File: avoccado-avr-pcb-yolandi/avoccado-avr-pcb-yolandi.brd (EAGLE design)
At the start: 50 x 50 mm, 55 parts, among them Q1 16MHz, Q2 FET, U2 MCP73831

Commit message: wip silkscreen
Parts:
- moved TP4 1.52 mm to (15.2, 27.4)
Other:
- board text added: "AO"
- board text added: "AVOCCADO YOLANDI"
- board text added: "CK"
- board text added: "ETEMU.COM 2O15"
- board text added: "MI"
- board text added: "MO"
- board text added: "RS"
- board text added: "V1"
- board text added: "VC"
- board text added: "VIBR"
- board text removed: "3V"
- board text removed: "AVOCCADO YOLANDI V1"
- board text removed: "RST"
- board text removed: "Vcc"
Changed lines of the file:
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@@
 <layer number="19" name="Unrouted" color="6" fill="1" visible="yes" active="yes"/>
 <layer number="20" name="Dimension" color="15" fill="1" visible="yes" active="yes"/>
-<layer number="21" name="tPlace" color="16" fill="1" visible="yes" active="yes"/>
+<layer number="21" name="tPlace" color="16" fill="1" visible="no" active="yes"/>
 <layer number="22" name="bPlace" color="14" fill="1" visible="yes" active="yes"/>
 <layer number="23" name="tOrigins" color="15" fill="1" visible="yes" active="yes"/>
@@
 <layer number="27" name="tValues" color="7" fill="1" visible="no" active="yes"/>
 <layer number="28" name="bValues" color="7" fill="1" visible="no" active="yes"/>
-<layer number="29" name="tStop" color="7" fill="3" visible="yes" active="yes"/>
-<layer number="30" name="bStop" color="7" fill="6" visible="yes" active="yes"/>
+<layer number="29" name="tStop" color="7" fill="3" visible="no" active="yes"/>
+<layer number="30" name="bStop" color="7" fill="6" visible="no" active="yes"/>
 <layer number="31" name="tCream" color="7" fill="4" visible="no" active="yes"/>
 <layer number="32" name="bCream" color="7" fill="5" visible="no" active="yes"/>
@@
 <wire x1="50" y1="50" x2="0" y2="50" width="0.2032" layer="20"/>
 <text x="27.026" y="15.584" size="0.8128" layer="21" ratio="12">9</text>
-<text x="10.414" y="23.114" size="0.8128" layer="21" ratio="12">8</text>
-<text x="12.954" y="23.114" size="0.8128" layer="21" ratio="12">7</text>
-<text x="15.494" y="23.114" size="0.8128" layer="21" ratio="12">6</text>
-<text x="18.034" y="23.114" size="0.8128" layer="21" ratio="12">5</text>
 <text x="26.899" y="21.272" size="0.8128" layer="21" ratio="12">4</text>
 <text x="22.835" y="25.336" size="0.8128" layer="21" ratio="12">VIB</text>
-<text x="21.844" y="14.224" size="0.8128" layer="21" ratio="12" rot="SR90">RX</text>
-<text x="21.844" y="11.684" size="0.8128" layer="21" ratio="12" rot="SR90">TX</text>
 <text x="32.972" y="38.931" size="0.8128" layer="21" ratio="12">BAT</text>
-<text x="20.066" y="18.288" size="0.8128" layer="21" ratio="12" rot="SR0">Vcc</text>
 <text x="37.059" y="28.892" size="0.8128" layer="21" ratio="12">A3</text>
 <text x="37.059" y="26.352" size="0.8128" layer="21" ratio="12">A2</text>
@@
 <text x="37.059" y="16.192" size="0.8128" layer="21" ratio="12">12</text>
 <text x="37.059" y="13.652" size="0.8128" layer="21" ratio="12">11</text>
-<text x="21.844" y="9.652" size="0.8128" layer="21" ratio="12" rot="R90">DT</text>
 <rectangle x1="3.912" y1="0.852" x2="6.452" y2="4.408" layer="25"/>
 <rectangle x1="15.35" y1="25.998" x2="18.906" y2="28.538" layer="25"/>
@@
 <circle x="14.732" y="23.622" radius="0.2032" width="0.4064" layer="29"/>
 <circle x="17.272" y="23.622" radius="0.2032" width="0.4064" layer="29"/>
-<text x="21.844" y="7.112" size="0.8128" layer="21" ratio="12" rot="SR90">3V</text>
-<text x="6.858" y="3.556" size="0.8128" layer="21" ratio="12" rot="SR0">Vb</text>
-<text x="14.986" y="2.032" size="0.8128" layer="21" ratio="12" rot="SR0">Vin</text>
-<text x="3.302" y="3.556" size="0.8128" layer="21" ratio="12" rot="SR0">VIB</text>
-<text x="9.271" y="22.352" size="0.508" layer="21" font="vector">AVOCCADO YOLANDI V1</text>
-<text x="10.414" y="11.43" size="0.6096" layer="21" font="vector">AVOCCADO YOLANDI V1</text>
-<text x="7.112" y="13.97" size="0.6096" layer="21" ratio="10" rot="SR0" align="center-left">RST</text>
+<text x="11.6078" y="22.352" size="0.508" layer="21" font="vector">ETEMU.COM 2O15</text>
+<text x="11.684" y="11.557" size="0.6096" layer="21" font="vector" align="center-left">AVOCCADO YOLANDI</text>
+<text x="7.112" y="13.97" size="0.6096" layer="21" ratio="10" rot="SR0" align="center-left">RS</text>
+<wire x1="6.858" y1="13.97" x2="6.604" y2="13.97" width="0.127" layer="21"/>
+<wire x1="6.604" y1="13.97" x2="6.35" y2="14.224" width="0.127" layer="21"/>
+<text x="7.112" y="16.51" size="0.6096" layer="21" ratio="10" rot="SR0" align="center-left">MO</text>
+<wire x1="6.858" y1="16.51" x2="6.604" y2="16.51" width="0.127" layer="21"/>
+<wire x1="6.604" y1="16.51" x2="6.35" y2="16.764" width="0.127" layer="21"/>
+<text x="7.112" y="19.05" size="0.6096" layer="21" ratio="10" rot="SR0" align="center-left">CK</text>
+<wire x1="6.858" y1="19.05" x2="6.604" y2="19.05" width="0.127" layer="21"/>
+<wire x1="6.604" y1="19.05" x2="6.35" y2="19.304" width="0.127" layer="21"/>
+<text x="7.112" y="21.59" size="0.6096" layer="21" ratio="10" rot="SR0" align="center-left">MI</text>
+<wire x1="6.858" y1="21.59" x2="6.604" y2="21.59" width="0.127" layer="21"/>
+<wire x1="6.604" y1="21.59" x2="6.35" y2="21.844" width="0.127" layer="21"/>
+<text x="7.112" y="11.557" size="0.6096" layer="21" ratio="10" rot="SR0" align="center-left">A3</text>
+<wire x1="6.858" y1="11.43" x2="6.604" y2="11.43" width="0.127" layer="21"/>
+<wire x1="6.604" y1="11.43" x2="6.35" y2="11.684" width="0.127" layer="21"/>
+<text x="4.572" y="11.557" size="0.6096" layer="21" ratio="10" rot="SR0" align="center-left">A1</text>
+<wire x1="4.318" y1="11.43" x2="4.064" y2="11.43" width="0.127" layer="21"/>
+<wire x1="4.064" y1="11.43" x2="3.81" y2="11.684" width="0.127" layer="21"/>
+<text x="2.032" y="11.557" size="0.6096" layer="21" ratio="10" rot="SR0" align="center-left">AO</text>
+<wire x1="1.778" y1="11.43" x2="1.524" y2="11.43" width="0.127" layer="21"/>
+<wire x1="1.524" y1="11.43" x2="1.27" y2="11.684" width="0.127" layer="21"/>
+<text x="21.59" y="15.24" size="0.6096" layer="21" ratio="10" rot="SR90" align="center-right">RX</text>
+<wire x1="21.59" y1="15.24" x2="21.59" y2="15.494" width="0.127" layer="21"/>
+<wire x1="21.59" y1="15.494" x2="21.844" y2="15.748" width="0.127" layer="21"/>
+<text x="9.652" y="11.557" size="0.6096" layer="21" ratio="10" rot="SR0" align="center-left">A2</text>
+<wire x1="9.398" y1="11.43" x2="9.144" y2="11.43" width="0.127" layer="21"/>
+<wire x1="9.144" y1="11.43" x2="8.89" y2="11.684" width="0.127" layer="21"/>
+<text x="22.86" y="23.114" size="0.6096" layer="21" ratio="10" rot="SR0" align="center-left">V1</text>
+<text x="10.414" y="23.368" size="0.6096" layer="21" ratio="10" rot="SR0" align="center-left">8</text>
+<text x="12.954" y="23.368" size="0.6096" layer="21" ratio="10" rot="SR0" align="center-left">7</text>
+<text x="15.494" y="23.368" size="0.6096" layer="21" ratio="10" rot="SR0" align="center-left">6</text>
+<text x="18.034" y="23.368" size="0.6096" layer="21" ratio="10" rot="SR0" align="center-left">5</text>
+<text x="25.654" y="15.24" size="0.6096" layer="21" ratio="10" rot="SR90" align="center-right">RX</text>
+<wire x1="25.654" y1="15.494" x2="25.908" y2="15.748" width="0.127" layer="21"/>
+<wire x1="25.654" y1="15.24" x2="25.654" y2="15.494" width="0.127" layer="21"/>
+<text x="21.59" y="12.7" size="0.6096" layer="21" ratio="10" rot="SR90" align="center-right">TX</text>
+<wire x1="21.59" y1="12.954" x2="21.844" y2="13.208" width="0.127" layer="21"/>
+<wire x1="21.59" y1="12.7" x2="21.59" y2="12.954" width="0.127" layer="21"/>
+<text x="21.59" y="10.16" size="0.6096" layer="21" ratio="10" rot="SR90" align="center-right">DT</text>
+<wire x1="21.59" y1="10.414" x2="21.844" y2="10.668" width="0.127" layer="21"/>
+<wire x1="21.59" y1="10.16" x2="21.59" y2="10.414" width="0.127" layer="21"/>
+<text x="21.59" y="7.62" size="0.6096" layer="21" ratio="10" rot="SR90" align="center-right">VC</text>
+<wire x1="21.59" y1="7.874" x2="21.844" y2="8.128" width="0.127" layer="21"/>
+<wire x1="21.59" y1="7.62" x2="21.59" y2="7.874" width="0.127" layer="21"/>
+<text x="21.59" y="17.78" size="0.6096" layer="21" ratio="10" rot="SR90" align="center-right">VC</text>
+<wire x1="21.59" y1="18.034" x2="21.844" y2="18.288" width="0.127" layer="21"/>
+<wire x1="21.59" y1="17.78" x2="21.59" y2="18.034" width="0.127" layer="21"/>
+<text x="17.78" y="3.81" size="0.6096" layer="21" ratio="10" rot="SR0" align="center-right">Vin</text>
+<wire x1="18.034" y1="3.81" x2="18.288" y2="3.556" width="0.127" layer="21"/>
+<wire x1="17.78" y1="3.81" x2="18.034" y2="3.81" width="0.127" layer="21"/>
+<text x="7.62" y="3.81" size="0.6096" layer="21" ratio="10" rot="SR0" align="center-right">Vb</text>
+<wire x1="7.874" y1="3.81" x2="8.128" y2="3.556" width="0.127" layer="21"/>
+<wire x1="7.62" y1="3.81" x2="7.874" y2="3.81" width="0.127" layer="21"/>
+<text x="5.08" y="3.81" size="0.6096" layer="21" ratio="10" rot="SR0" align="center-right">VIBR</text>
+<wire x1="5.334" y1="3.81" x2="5.588" y2="3.556" width="0.127" layer="21"/>
+<wire x1="5.08" y1="3.81" x2="5.334" y2="3.81" width="0.127" layer="21"/>
 </plain>
 <attributes>
@@
 <element name="TP2" library="SparkFun-Passives" package="PAD.03X.04" value="TEST-POINT3X4" x="26.416" y="11.684"/>
 <element name="TP3" library="SparkFun-Passives" package="PAD.03X.03" value="TEST-POINT3" x="26.924" y="10.668"/>
-<element name="TP4" library="SparkFun-Passives" package="PAD.02X.02" value="TEST-POINT2" x="15.24" y="25.908"/>
+<element name="TP4" library="SparkFun-Passives" package="PAD.02X.02" value="TEST-POINT2" x="15.24" y="27.432"/>
 <element name="TP5" library="SparkFun-Passives" package="TP_15TH" value="TEST-POINTTP_15TH_THRU" x="7.112" y="27.94"/>
 <element name="LOGO1" library="SparkFun-Aesthetics" package="OSHW-LOGO-S" value="OSHW-LOGOS" x="27.432" y="2.54"/>

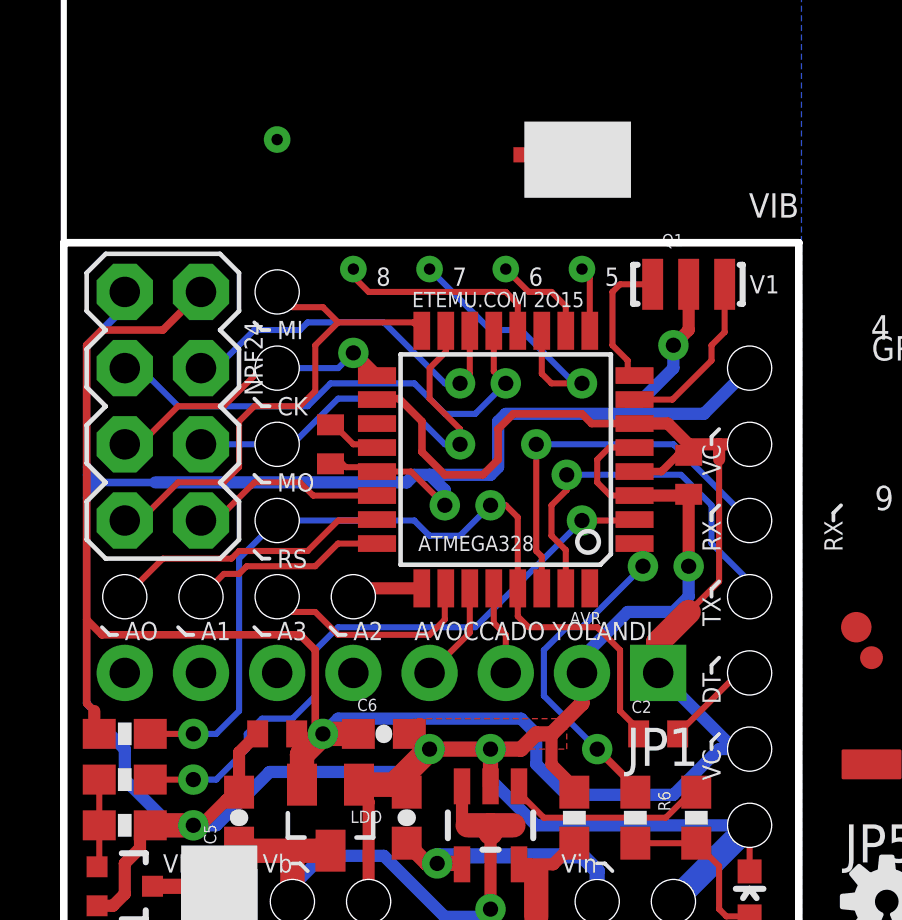
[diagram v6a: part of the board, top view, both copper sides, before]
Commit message: change pkg of NRF24 header to round pins
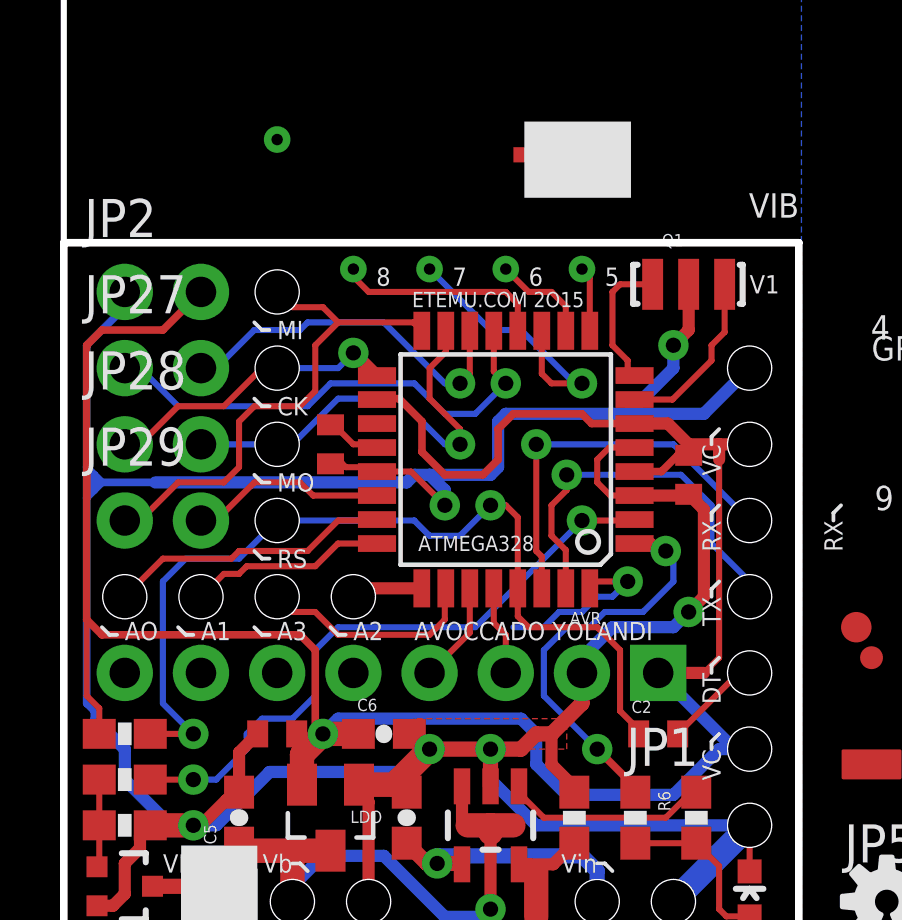
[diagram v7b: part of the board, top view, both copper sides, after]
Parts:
- removed NRF24: M04X2, SparkFun-Connectors:2X4
- added JP2, JP27, JP28, JP29: M021X02_NO_SILK, SparkFun-Connectors:1X02_NO_SILK
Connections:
- net 3V3: now also JP2.2; no longer NRF24.2
- net A7: now also JP29.2; no longer NRF24.8
- net D10: now also JP27.2; no longer NRF24.4
- net D9: now also JP27.1; no longer NRF24.3
- net GND: now also JP2.1; no longer NRF24.1
- net MISO: now also JP29.1; no longer NRF24.7
- net MOSI: now also JP28.2; no longer NRF24.6
- net SCK: now also JP28.1; no longer NRF24.5
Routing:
- net D2: track 0.00 -> 5.80 mm, vias 0 -> 1
- net D3: track 11.8 -> 14.0 mm
- net RESET: track 29.2 -> 30.6 mm
- net 3V3: track 79.5 -> 80.4 mm
- net GND: track 125.6 -> 126.3 mm

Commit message: schematic cleanup
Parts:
- removed JP16, JP7: M01POGOPIN_HOLE_0.58, SparkFun-Connectors:1X01_POGOPIN_HOLE_0.58
- removed JP4: (no value), SparkFun-Connectors:1X08_PIN1_NO_SILK
- removed JP5: M01SMD, SparkFun-Connectors:LUXEON-PAD
- removed TP2: TEST-POINT3X4, SparkFun-Passives:PAD.03X.04
- removed TP3: TEST-POINT3, SparkFun-Passives:PAD.03X.03
- removed TP4: TEST-POINT2, SparkFun-Passives:PAD.02X.02
- removed TP5: TEST-POINTTP_15TH_THRU, SparkFun-Passives:TP_15TH
- removed U$1: AVR_MINI_PROGSMD, SparkFun-Connectors:AVR_MINI_PROG
- JP1: value (none) -> MPU6050
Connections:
- net A7 renamed A7-NRF-IRQ
- removed net 3V3: AVR.18, AVR.4, AVR.6, C10.1, C3.2, C6.1, JP1.1, JP11.1, JP16.1, JP18.1, JP2.2, LDO.2, R2.2
- new net 3.3V: AVR.18, AVR.4, AVR.6, C10.1, C3.2, C6.1, JP1.1, JP11.1, JP18.1, JP2.2, LDO.2, R2.2
- net VBAT: no longer JP7.1
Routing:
- net 3.3V: track 0.00 -> 81.3 mm, vias 0 -> 1
- net 3V3: track 80.4 -> 0.00 mm, vias 1 -> 0
- net D2: track 5.80 -> 9.10 mm
- net D4: track 20.9 -> 23.7 mm
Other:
- board size 50 x 50 mm -> 50 x 49 mm
- board text removed: "11"
- board text removed: "12"
- board text removed: "13"
- board text removed: "4"
- board text removed: "9"
- board text removed: "A0"
- board text removed: "BAT"
- board text removed: "GROUND"
- board text removed: "VIB"
- board text removed: "avoccado"
